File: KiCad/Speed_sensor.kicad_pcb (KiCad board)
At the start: 4 copper layers, 69 parts, among them J1 USB_B_Micro, J2 SWD, U1 BQ24040, U2 TP1941U, U3 ST1PS02, U4 nRF52832-QFxx, U5 LIS2DH12, Y1 32,768kHz, Y2 32MHz

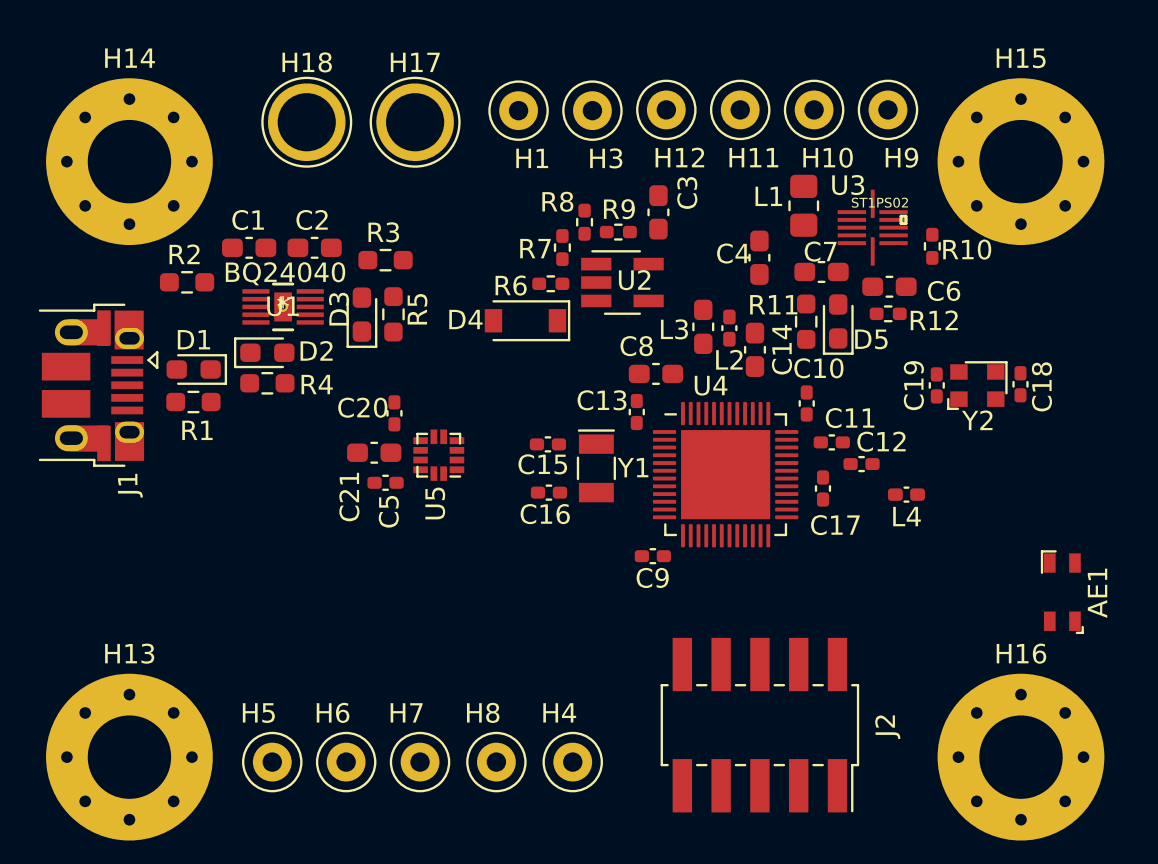
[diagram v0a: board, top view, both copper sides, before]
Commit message: changed which GPIO pins are used for SPI
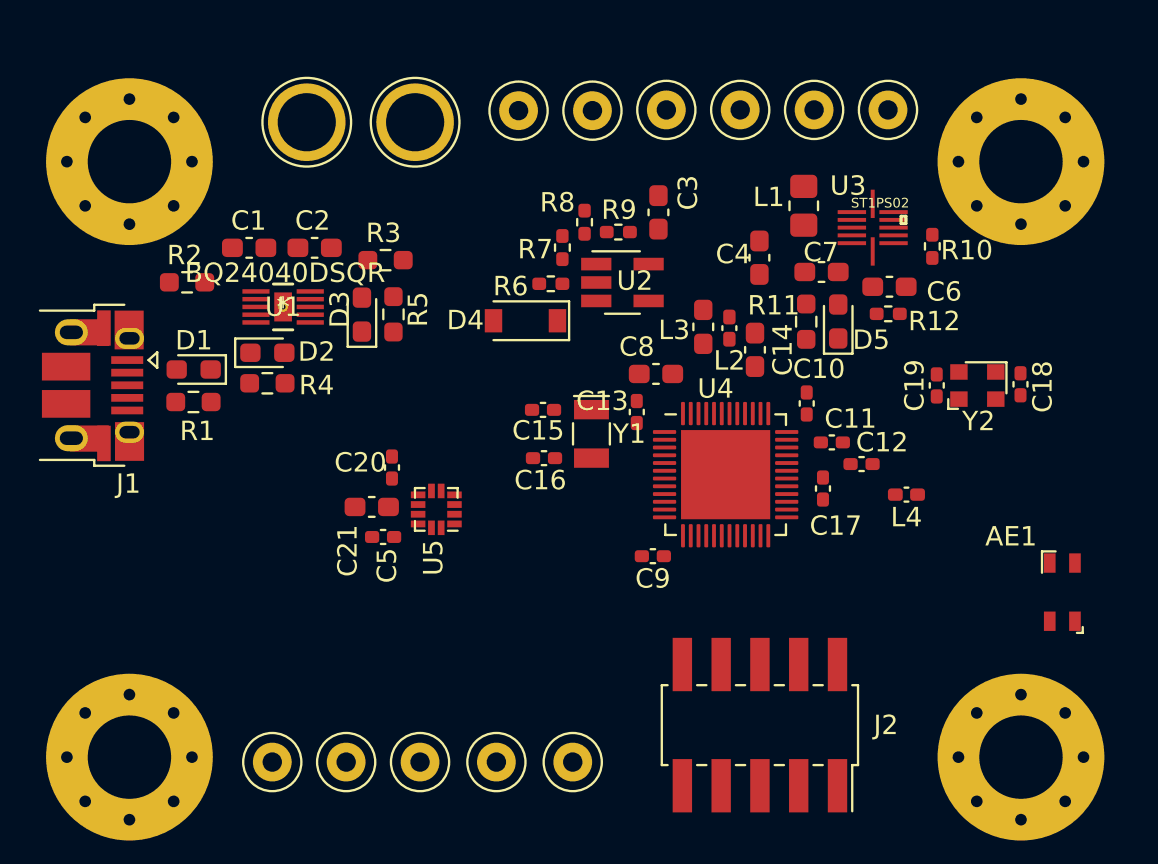
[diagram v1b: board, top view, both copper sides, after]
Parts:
- U1: value BQ24040 -> BQ24040DSQR
- moved C5 2.80 mm to (111.6, 62.6)
- moved C21 2.80 mm to (111.0, 61.1)
- moved C20 2.80 mm to (112.1, 59.1)
- moved U5 2.80 mm to (114.4, 61.2)
- moved C15 1.80 mm to (119.9, 56.1)
- moved C16 1.80 mm to (119.9, 58.6)
- moved Y1 1.80 mm to (122.4, 57.3)
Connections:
- U4 pad 10: ACCEL_INT2 -> Net-(U4-Pad10)
- U4 pad 16: SPI_01_CS -> SPI_MOSI
- U4 pad 18: SPI_SCK -> SPI_01_CS
- U4 pad 19: SPI_MOSI -> SPI_SCK
- U4 pad 8: Net-(U4-Pad8) -> ACCEL_INT1
- U4 pad 9: ACCEL_INT1 -> ACCEL_INT2

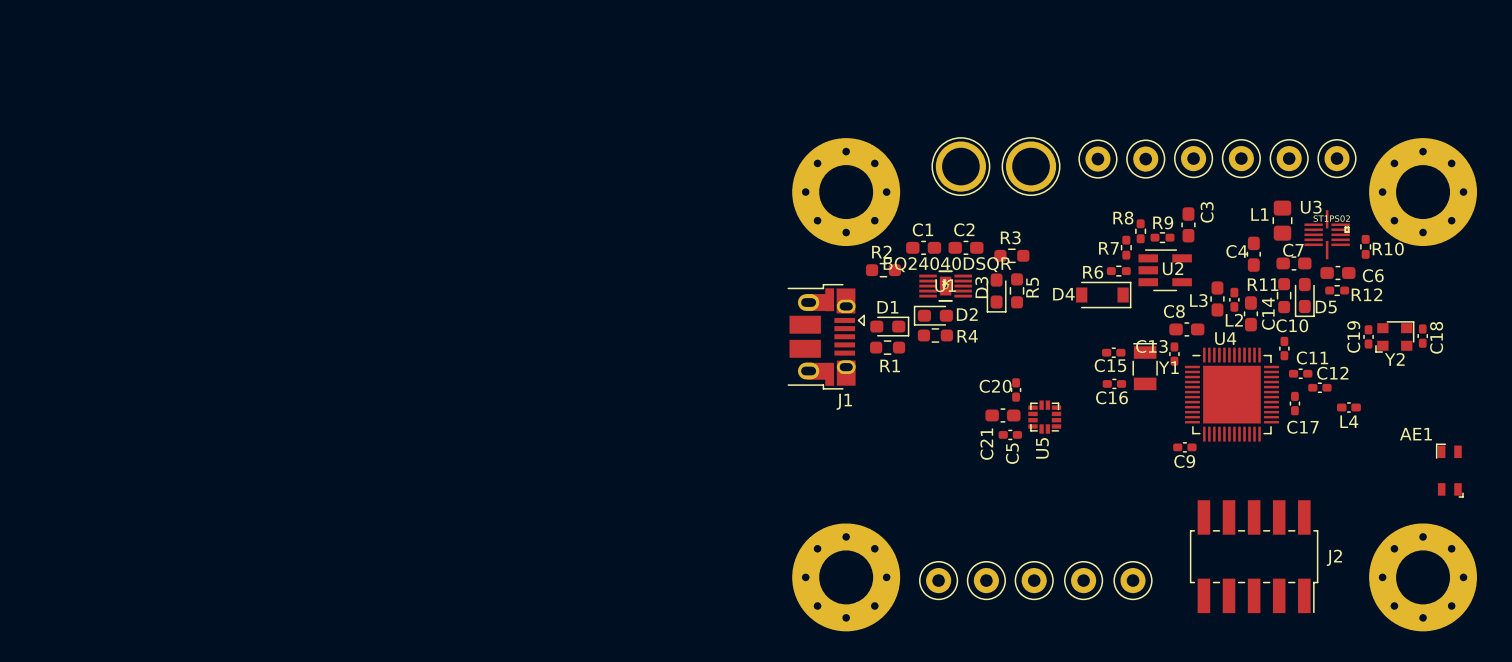
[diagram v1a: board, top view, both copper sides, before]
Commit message: layout part positions changed slightly, added 3,5cm x 2cm outline (as a goal)
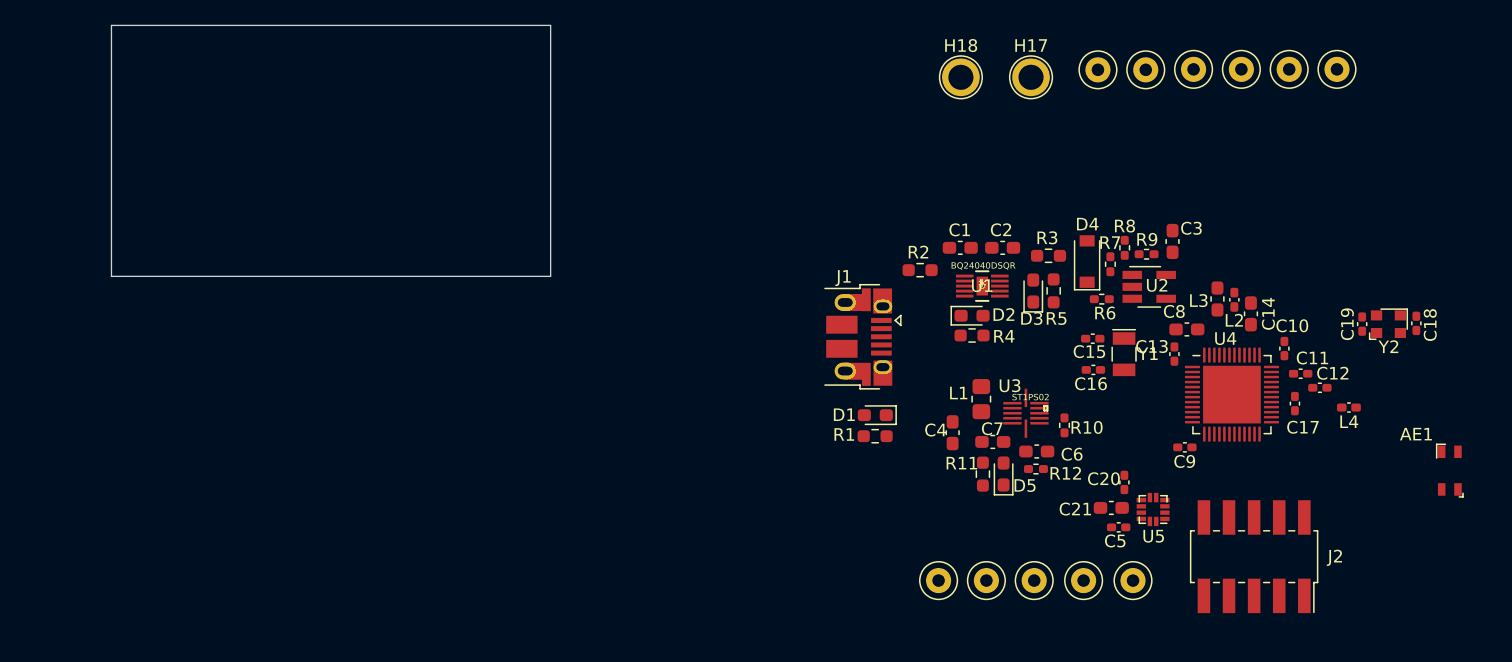
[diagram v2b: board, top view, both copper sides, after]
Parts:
- removed H13, H14, H15, H16: MountingHole_Pad, MountingHole:MountingHole_4.3mm_M4_Pad_Via
- H17, H18: footprint TestPoint:TestPoint_Plated_Hole_D3.0mm -> TestPoint:TestPoint_Plated_Hole_D2.0mm
- moved R10 27.9 mm to (116.0, 61.9)
- moved R11 27.9 mm to (109.4, 65.8)
- moved R12 27.9 mm to (113.7, 65.4)
- moved C7 27.9 mm to (110.2, 63.2)
- moved C6 27.9 mm to (113.7, 64.0)
- moved D5 27.9 mm to (111.1, 65.7)
- moved L1 27.9 mm to (109.3, 59.8)
- moved C4 27.9 mm to (107.0, 62.5)
- moved U3 27.9 mm to (112.9, 60.9)
- moved C20 11.4 mm to (120.7, 66.4)
- moved U5 11.4 mm to (123.0, 68.6)
- moved C5 11.4 mm to (120.3, 70.0)
- moved C21 11.4 mm to (119.7, 68.5)
- moved D1 7.13 mm to (100.9, 61.1)
- moved R1 7.13 mm to (100.9, 62.7)
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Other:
- board outline added: 35 x 20 mm

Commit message: defined PCB size 35mm x 20mm, started rearranging layout (starting with power circuit (5V + Batt low voltage turn OFF)
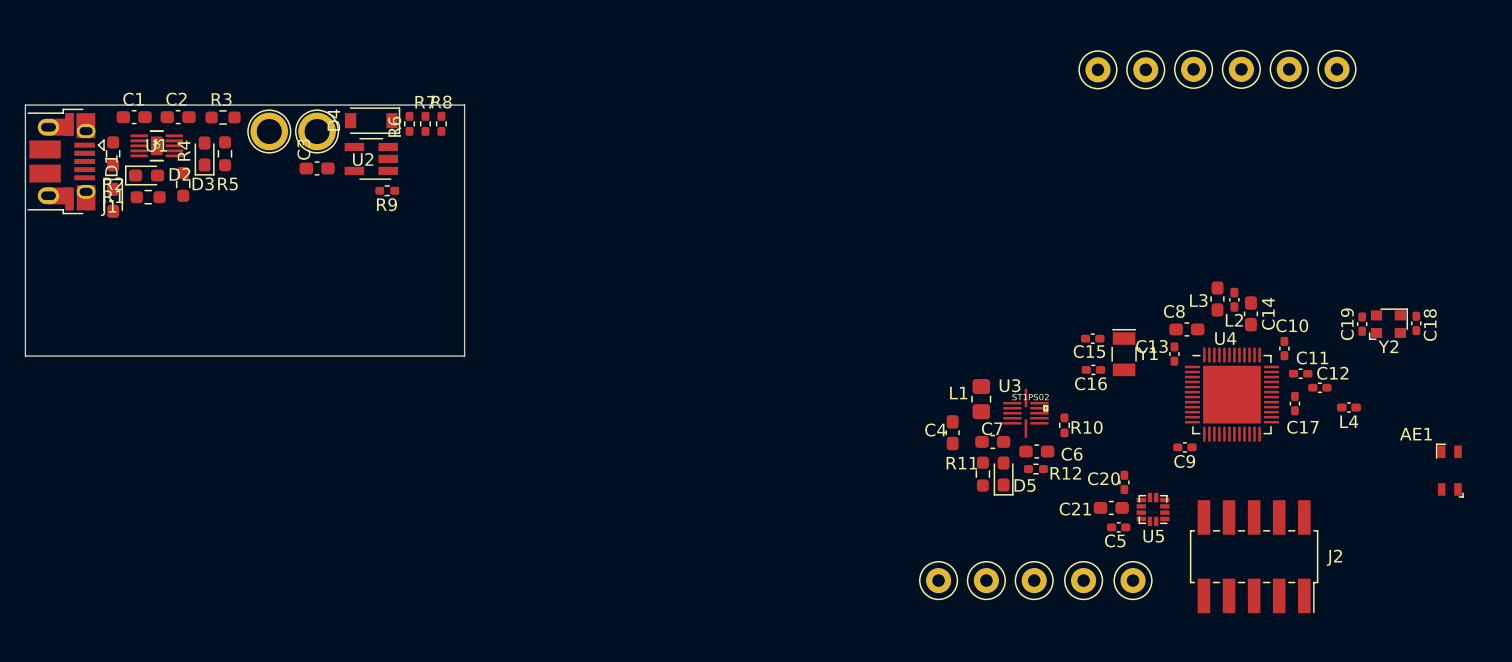
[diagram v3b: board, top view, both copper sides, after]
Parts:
- D2: value IN -> IN-GREEN
- D3: value charging -> charging-ORANGE
- R4: value 1,5k -> 510
- R5: value 1,5k -> 270
- moved C3 68.4 mm to (56.4, 41.4), turned to 180 degrees
- moved D3 66.9 mm to (47.4, 40.2)
- moved R5 66.9 mm to (49.0, 40.2)
- moved D2 66.7 mm to (42.8, 42.0)
- moved U1 66.7 mm to (43.6, 39.6)
- moved R3 66.7 mm to (48.9, 37.3)
- moved C1 66.7 mm to (41.8, 37.3)
- moved C2 66.5 mm to (45.3, 37.3)
- moved J1 65.0 mm to (36.1, 40.9)
- moved R2 65.0 mm to (40.1, 40.2), turned to 270 degrees
- moved R4 64.0 mm to (45.7, 42.7), turned to 270 degrees
- moved D1 63.1 mm to (40.1, 43.9), turned to 270 degrees
- moved U2 62.8 mm to (60.7, 40.6), turned to 180 degrees
- moved R1 61.0 mm to (42.9, 43.7), turned to 0 degrees
- moved H17 60.9 mm to (52.6, 38.5)
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
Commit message: added Buck converter part to the properly sized layout
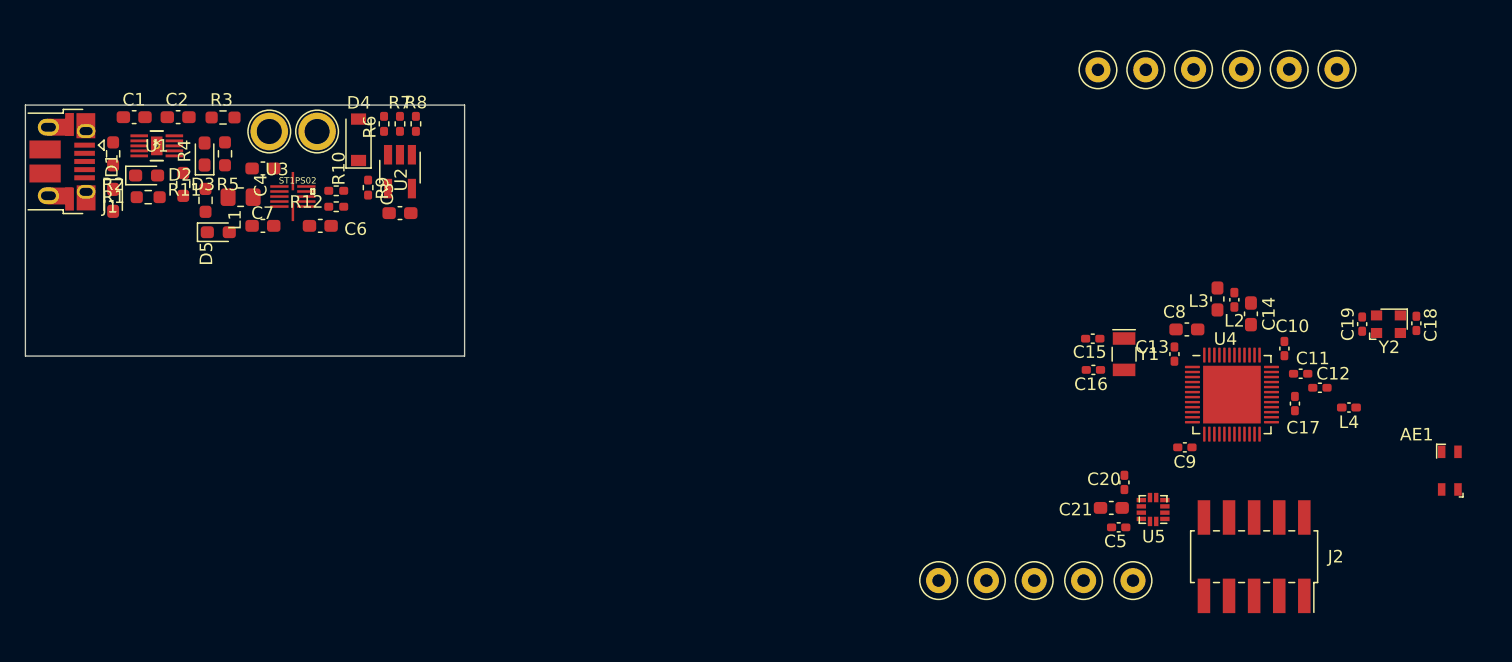
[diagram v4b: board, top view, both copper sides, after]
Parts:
- moved R11 65.7 mm to (47.5, 43.9)
- moved D5 65.5 mm to (48.5, 46.5), turned to 0 degrees
- moved L1 61.2 mm to (50.3, 43.7), turned to 180 degrees
- moved R10 61.0 mm to (57.9, 43.2), turned to 0 degrees
- moved U3 60.9 mm to (54.5, 43.6)
- moved C7 60.7 mm to (52.1, 46.0)
- moved C6 59.9 mm to (56.6, 46.0)
- moved R12 59.6 mm to (57.9, 44.5), turned to 0 degrees
- moved C4 58.9 mm to (52.1, 41.4), turned to 0 degrees
- moved C3 7.50 mm to (63.0, 45.0)
- moved U2 2.50 mm to (63.0, 41.7), turned to 270 degrees
- moved R7 2.03 mm to (63.0, 37.8)
- moved R6 2.03 mm to (61.7, 37.8)
- moved R8 2.03 mm to (64.3, 37.8)
- moved D4 1.83 mm to (59.7, 39.1), turned to 90 degrees
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
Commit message: Bauteilbezeichnungen auf nicht mehr sichtbar gemacht
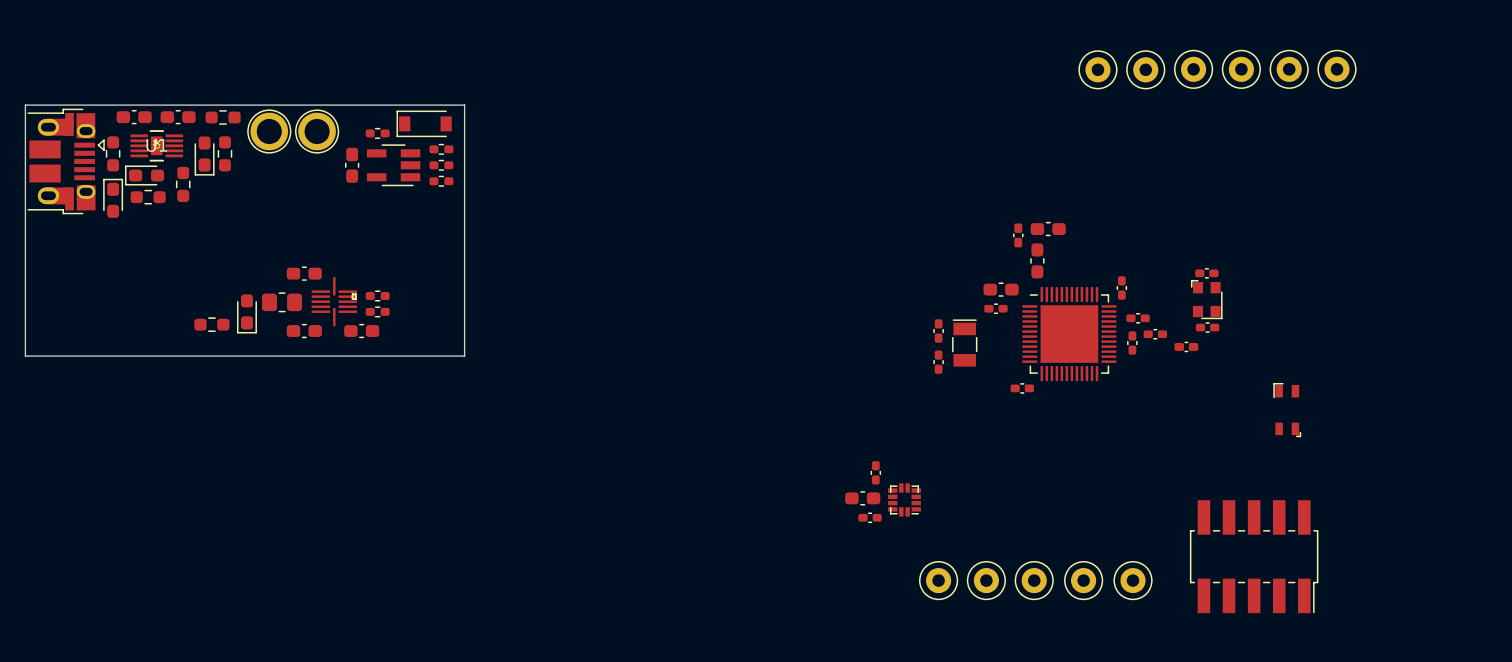
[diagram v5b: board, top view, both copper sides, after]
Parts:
- moved C20 19.8 mm to (100.9, 65.7)
- moved C5 19.8 mm to (100.5, 69.2)
- moved U5 19.8 mm to (103.2, 67.8)
- moved C21 19.8 mm to (99.9, 67.7)
- moved L2 18.0 mm to (112.3, 46.7), turned to 90 degrees
- moved C14 17.5 mm to (114.7, 46.2), turned to 0 degrees
- moved C18 16.6 mm to (127.4, 54.1), turned to 180 degrees
- moved C8 15.1 mm to (110.9, 51.1)
- moved C13 14.7 mm to (110.5, 52.6), turned to 180 degrees
- moved L3 14.7 mm to (113.8, 48.8)
- moved Y2 14.6 mm to (127.3, 51.9), turned to 90 degrees
- moved C10 13.8 mm to (120.5, 50.9)
- moved C17 13.8 mm to (121.4, 55.3)
- moved L4 13.8 mm to (125.7, 55.6)
- moved AE1 13.8 mm to (133.8, 60.7)
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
